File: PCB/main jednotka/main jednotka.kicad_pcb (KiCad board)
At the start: 2 copper layers, 4 parts, among them J1 USB4105-GF-A, U1 ESP32-S3-WROOM-1-N16R2

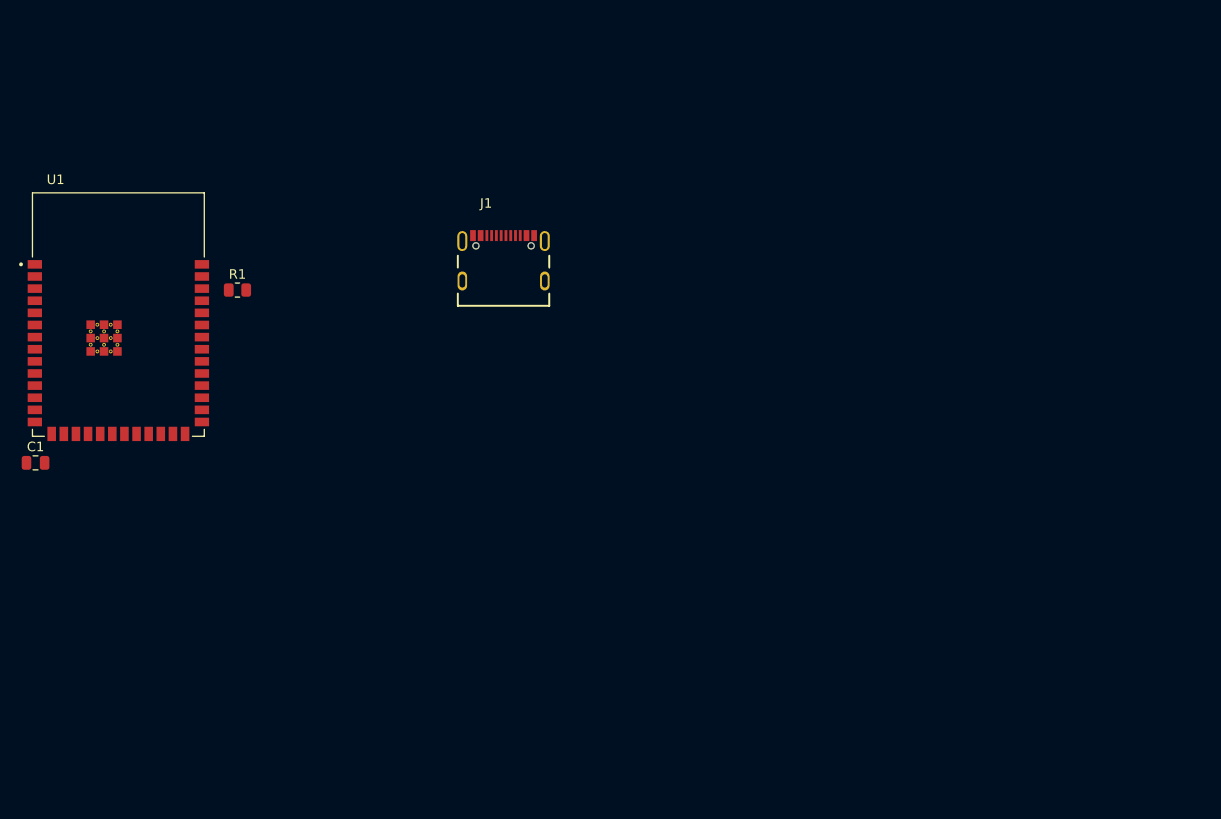
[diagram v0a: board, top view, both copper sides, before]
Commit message: Main jednotka V1 a objednavka jlcpcb
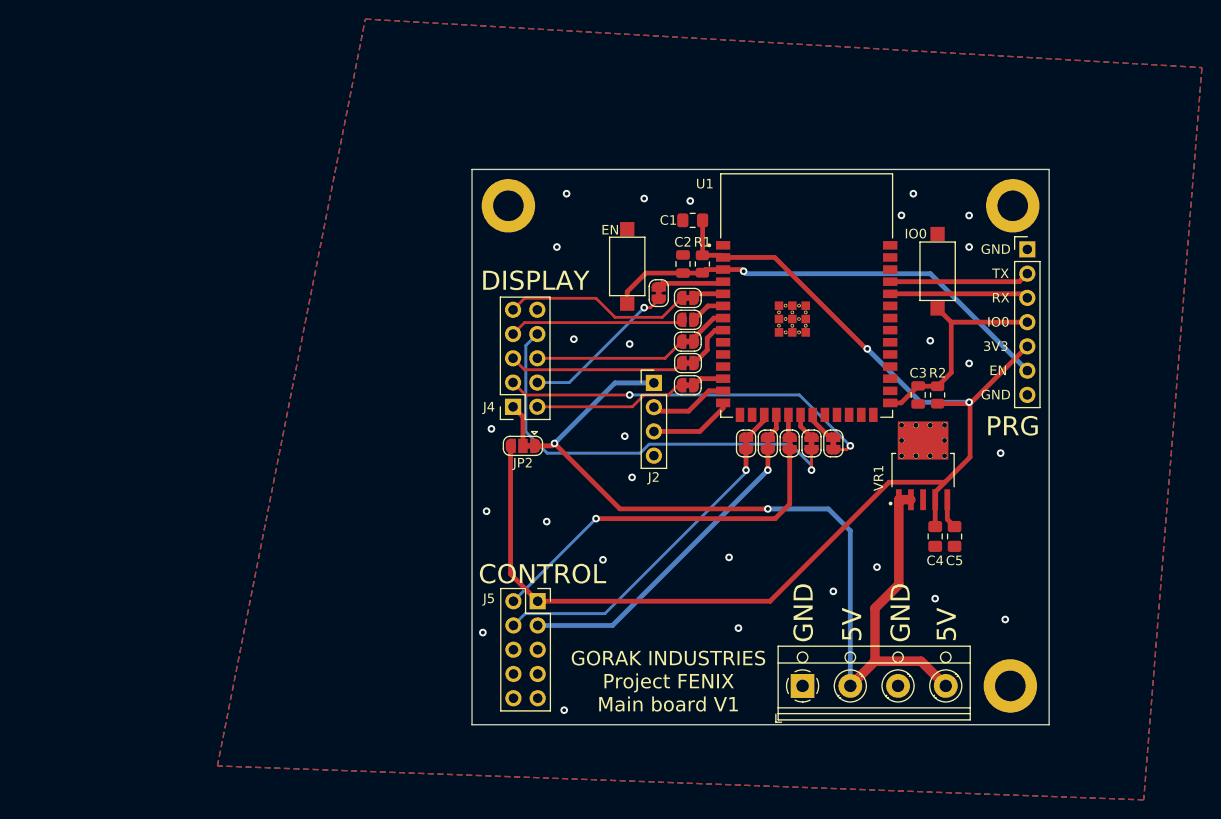
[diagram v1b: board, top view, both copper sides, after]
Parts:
- added ?: , , F.Cu at (169.7, 68.6)
- added ?: , , F.Cu at (222.5, 68.6)
- added C1: 100nF, Capacitor_SMD:C_0805_2012Metric_Pad1.18x1.45mm_HandSolder, F.Cu at (189.0, 70.1)
- added C3: 470nF, Capacitor_SMD:C_0805_2012Metric, F.Cu at (212.6, 88.4)
- added C4: 1uF, Capacitor_SMD:C_0805_2012Metric_Pad1.18x1.45mm_HandSolder, F.Cu at (214.4, 103.2)
- added C5: 10nF, Capacitor_SMD:C_0805_2012Metric_Pad1.18x1.45mm_HandSolder, F.Cu at (216.4, 103.2)
- added EN: EN, Button_Switch_SMD:SW_SPST_CK_RS282G05A3, F.Cu at (182.1, 74.9)
- added IO0: IO0, Button_Switch_SMD:SW_SPST_CK_RS282G05A3, F.Cu at (214.6, 75.4)
- added J2: USB_B, Connector_PinHeader_2.54mm:PinHeader_1x04_P2.54mm_Vertical, F.Cu at (184.9, 87.1)
- added J3: VIN, TerminalBlock_RND:TerminalBlock_RND_205-00014_1x04_P5.00mm_Horizontal, F.Cu at (200.5, 118.9)
- added J4: Display, Connector_PinSocket_2.54mm:PinSocket_2x05_P2.54mm_Vertical, F.Cu at (170.2, 89.6)
- added J5: Control, Connector_PinSocket_2.54mm:PinSocket_2x05_P2.54mm_Vertical, F.Cu at (172.7, 110.0)
- added JP1: SolderJumper_2_Bridged, Jumper:SolderJumper-2_P1.3mm_Bridged_RoundedPad1.0x1.5mm, F.Cu at (185.4, 77.7)
- added JP10: SolderJumper_2_Bridged, Jumper:SolderJumper-2_P1.3mm_Bridged_RoundedPad1.0x1.5mm, F.Cu at (201.4, 93.5)
- added JP11: SolderJumper_2_Bridged, Jumper:SolderJumper-2_P1.3mm_Bridged_RoundedPad1.0x1.5mm, F.Cu at (203.7, 93.5)
- added JP12: SolderJumper_2_Bridged, Jumper:SolderJumper-2_P1.3mm_Bridged_RoundedPad1.0x1.5mm, F.Cu at (188.5, 85.1)
- added JP2: SolderJumper_3_Bridged12, Jumper:SolderJumper-3_P1.3mm_Bridged12_RoundedPad1.0x1.5mm, F.Cu at (171.2, 93.7)
- added JP3: SolderJumper_2_Bridged, Jumper:SolderJumper-2_P1.3mm_Bridged_RoundedPad1.0x1.5mm, F.Cu at (188.5, 78.2)
- added JP4: jumper, Jumper:SolderJumper-2_P1.3mm_Open_RoundedPad1.0x1.5mm, F.Cu at (188.5, 80.5)
- added JP5: SolderJumper_2_Bridged, Jumper:SolderJumper-2_P1.3mm_Bridged_RoundedPad1.0x1.5mm, F.Cu at (188.5, 82.8)
- added JP6: SolderJumper_2_Bridged, Jumper:SolderJumper-2_P1.3mm_Bridged_RoundedPad1.0x1.5mm, F.Cu at (188.5, 87.4)
- added JP7: SolderJumper_2_Bridged, Jumper:SolderJumper-2_P1.3mm_Bridged_RoundedPad1.0x1.5mm, F.Cu at (194.6, 93.5)
- added JP8: SolderJumper_2_Bridged, Jumper:SolderJumper-2_P1.3mm_Bridged_RoundedPad1.0x1.5mm, F.Cu at (196.8, 93.5)
- added JP9: SolderJumper_2_Bridged, Jumper:SolderJumper-2_P1.3mm_Bridged_RoundedPad1.0x1.5mm, F.Cu at (199.1, 93.5)
- added R2: 10k, Resistor_SMD:R_0805_2012Metric, F.Cu at (214.6, 88.4)
- added REF**: MountingHole_3.2mm_M3_DIN965_Pad, MountingHole:MountingHole_3.2mm_M3_DIN965_Pad, F.Cu at (222.2, 118.9)
- added VR1: TPS79633DCQ, TPS79633DCQ:VREG_TPS79633DCQ, F.Cu at (213.1, 96.3)
- J1: value USB4105-GF-A -> PRG_header; footprint USB-C better:GCT_USB4105-GF-A -> Connector_PinHeader_2.54mm:PinHeader_1x07_P2.54mm_Vertical
- moved U1 72.1 mm to (200.9, 78.0)
- moved C2 70.9 mm to (188.0, 74.7), turned to 90 degrees
- moved J1 55.0 mm to (224.0, 73.1)
- moved R1 48.8 mm to (190.0, 74.7), turned to -90 degrees
- renumbered C1 to C2
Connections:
- U1 pad 12: unconnected-(U1-Pad12) -> Net-(U1-Pad12)
- U1 pad 17: unconnected-(U1-Pad17) -> Net-(U1-Pad17)
- U1 pad 18: unconnected-(U1-Pad18) -> Net-(U1-Pad18)
- U1 pad 19: unconnected-(U1-Pad19) -> Net-(U1-Pad19)
- U1 pad 20: unconnected-(U1-Pad20) -> Net-(U1-Pad20)
- U1 pad 21: unconnected-(U1-Pad21) -> Net-(U1-Pad21)
- U1 pad 4: unconnected-(U1-Pad4) -> Net-(U1-Pad4)
- U1 pad 41_10: (no net) -> GND
- U1 pad 41_11: (no net) -> GND
- U1 pad 41_12: (no net) -> GND
- U1 pad 41_13: (no net) -> GND
- U1 pad 41_14: (no net) -> GND
- U1 pad 41_15: (no net) -> GND
- U1 pad 41_16: (no net) -> GND
- U1 pad 41_17: (no net) -> GND
- U1 pad 41_18: (no net) -> GND
- U1 pad 41_19: (no net) -> GND
- U1 pad 41_20: (no net) -> GND
- U1 pad 41_21: (no net) -> GND
- U1 pad 5: unconnected-(U1-Pad5) -> Net-(U1-Pad5)
- U1 pad 6: unconnected-(U1-Pad6) -> Net-(U1-Pad6)
- U1 pad 7: unconnected-(U1-Pad7) -> Net-(U1-Pad7)
- U1 pad 8: unconnected-(U1-Pad8) -> Net-(U1-Pad8)
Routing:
- net +3.3V: track 0.00 -> 129.5 mm, vias 0 -> 2
- net +5V: track 0.00 -> 97.5 mm, vias 0 -> 2
- net EN: track 0.00 -> 48.5 mm, vias 0 -> 1
- net SCK: track 0.00 -> 45.5 mm, vias 0 -> 1
- net CS: track 0.00 -> 40.0 mm, vias 0 -> 2
- net INT: track 0.00 -> 38.9 mm, vias 0 -> 1
- net SCL: track 0.00 -> 33.4 mm, vias 0 -> 1
- net SDA: track 0.00 -> 33.0 mm, vias 0 -> 1
- net IO0: track 0.00 -> 23.0 mm
- net MOSI: track 0.00 -> 19.8 mm
- net DC/RS: track 0.00 -> 18.5 mm
- net MISO: track 0.00 -> 18.3 mm
- net RESET: track 0.00 -> 16.3 mm, vias 0 -> 1
- net N_out: track 0.00 -> 16.1 mm
- net LED_back: track 0.00 -> 15.8 mm
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- added copper zone on B.Cu, net GND
- added copper zone on F.Cu, net GND
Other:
- board outline added: 60.5 x 58.2 mm
- board text added: "3V3"
- board text added: "5V"
- board text added: "CONTROL"
- board text added: "DISPLAY"
- board text added: "EN"
- board text added: "GND"
- board text added: "GORAK INDUSTRIES Project FENIX Main board V1"
- board text added: "IO0"
- board text added: "PRG"
- board text added: "RX"
- board text added: "TX"
